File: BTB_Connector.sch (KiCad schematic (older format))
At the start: 2 parts, among them J5 BoardEdge_of_HSEC8-140-01-L-P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, J6 BoardEdge_of_HSEC8-140-01-L-P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

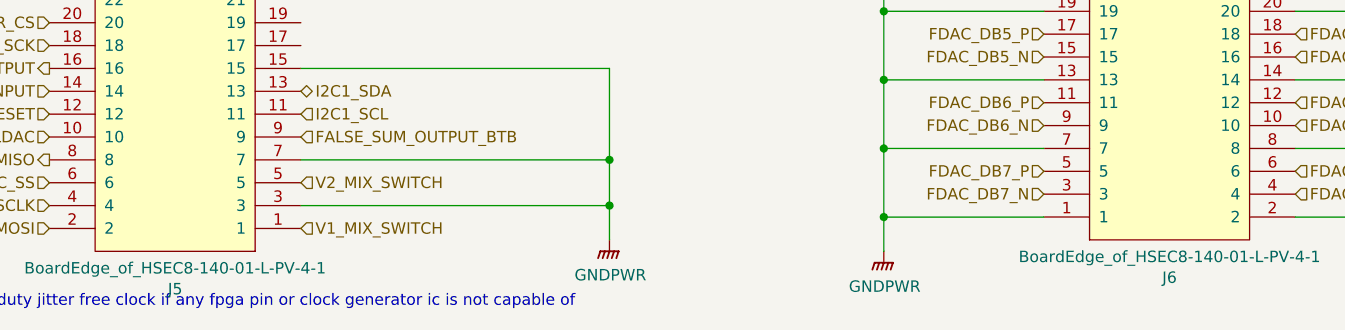
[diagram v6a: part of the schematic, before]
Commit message: Corrected PCB import errors
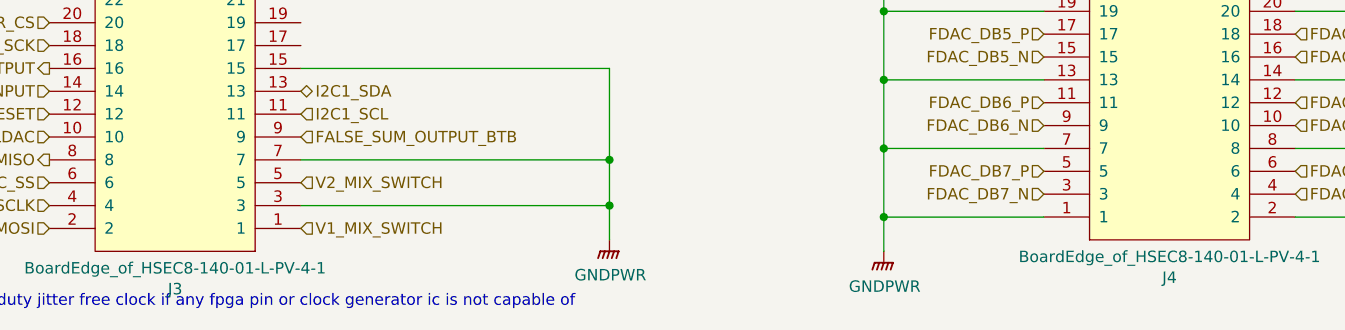
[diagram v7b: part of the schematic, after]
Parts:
- J4: renamed from J6; footprint GM_Connectors:HSEC8-140-01-L-PV-4-1 -> GM_Connectors:BoardEdge_of_HSEC8-140-01-L-PV-4-1
- renumbered J5 to J3
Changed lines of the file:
@@
 P 2550 1500
 AR Path="/60256C5F/602FF0E5" Ref="#PWR?"  Part="1"
-AR Path="/601E7B79/602FF0E5" Ref="#PWR065"  Part="1"
-F 0 "#PWR065" H 2550 1300 50  0001 C CNN
+AR Path="/601E7B79/602FF0E5" Ref="#PWR029"  Part="1"
+F 0 "#PWR029" H 2550 1300 50  0001 C CNN
 F 1 "GNDPWR" H 2554 1346 50  0000 C CNN
 F 2 "" H 2550 1450 50  0001 C CNN
@@
 	4200 1500 4200 1750
 $Comp
-L GM_Connectors:BoardEdge_of_HSEC8-140-01-L-PV-4-1 J6
+L GM_Connectors:BoardEdge_of_HSEC8-140-01-L-PV-4-1 J4
 U 1 1 605943E0
 P 7650 6100
-F 0 "J6" H 8000 6265 50  0000 C CNN
+F 0 "J4" H 8000 6265 50  0000 C CNN
 F 1 "BoardEdge_of_HSEC8-140-01-L-PV-4-1" H 8000 6174 50  0000 C CNN
-F 2 "GM_Connectors:HSEC8-140-01-L-PV-4-1" H 7650 6100 50  0001 C CNN
+F 2 "GM_Connectors:BoardEdge_of_HSEC8-140-01-L-PV-4-1" H 7650 6100 50  0001 C CNN
 F 3 "http://suddendocs.samtec.com/prints/hsec8-1xx-xx-x-pv-x-x-xx-footprint.pdf" H 7650 6100 50  0001 C CNN
 	1    7650 6100
@@
 P 6500 1450
 AR Path="/60256C5F/6059456A" Ref="#PWR?"  Part="1"
-AR Path="/601E7B79/6059456A" Ref="#PWR067"  Part="1"
-F 0 "#PWR067" H 6500 1250 50  0001 C CNN
+AR Path="/601E7B79/6059456A" Ref="#PWR031"  Part="1"
+F 0 "#PWR031" H 6500 1250 50  0001 C CNN
 F 1 "GNDPWR" H 6504 1296 50  0000 C CNN
 F 2 "" H 6500 1400 50  0001 C CNN
@@
 	8550 1450 7450 1450
 $Comp
-L GM_Connectors:BoardEdge_of_HSEC8-140-01-L-PV-4-1 J5
+L GM_Connectors:BoardEdge_of_HSEC8-140-01-L-PV-4-1 J3
 U 1 1 602EB3A8
 P 4000 6150
-F 0 "J5" H 4350 6315 50  0000 C CNN
+F 0 "J3" H 4350 6315 50  0000 C CNN
 F 1 "BoardEdge_of_HSEC8-140-01-L-PV-4-1" H 4350 6224 50  0000 C CNN
 F 2 "GM_Connectors:BoardEdge_of_HSEC8-140-01-L-PV-4-1" H 4000 6150 50  0001 C CNN
@@
 P 5550 6100
 AR Path="/60256C5F/6055F126" Ref="#PWR?"  Part="1"
-AR Path="/601E7B79/6055F126" Ref="#PWR066"  Part="1"
-F 0 "#PWR066" H 5550 5900 50  0001 C CNN
+AR Path="/601E7B79/6055F126" Ref="#PWR030"  Part="1"
+F 0 "#PWR030" H 5550 5900 50  0001 C CNN
 F 1 "GNDPWR" H 5554 5946 50  0000 C CNN
 F 2 "" H 5550 6050 50  0001 C CNN
@@
 P 9250 6150
 AR Path="/60256C5F/605A0A6D" Ref="#PWR?"  Part="1"
-AR Path="/601E7B79/605A0A6D" Ref="#PWR0218"  Part="1"
-F 0 "#PWR0218" H 9250 5950 50  0001 C CNN
+AR Path="/601E7B79/605A0A6D" Ref="#PWR033"  Part="1"
+F 0 "#PWR033" H 9250 5950 50  0001 C CNN
 F 1 "GNDPWR" H 9254 5996 50  0000 C CNN
 F 2 "" H 9250 6100 50  0001 C CNN
@@
 P 6750 6150
 AR Path="/60256C5F/605A11CE" Ref="#PWR?"  Part="1"
-AR Path="/601E7B79/605A11CE" Ref="#PWR0219"  Part="1"
-F 0 "#PWR0219" H 6750 5950 50  0001 C CNN
+AR Path="/601E7B79/605A11CE" Ref="#PWR032"  Part="1"
+F 0 "#PWR032" H 6750 5950 50  0001 C CNN
 F 1 "GNDPWR" H 6754 5996 50  0000 C CNN
 F 2 "" H 6750 6100 50  0001 C CNN
